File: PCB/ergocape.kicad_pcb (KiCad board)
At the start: 2 copper layers, 183.2 x 140.8 mm, 94 parts, among them J1 AudioJack4, J2 AudioJack4, SW1 SW_PUSH, U1 ATMEGA32U4, X1 Crystal_GND24_Small

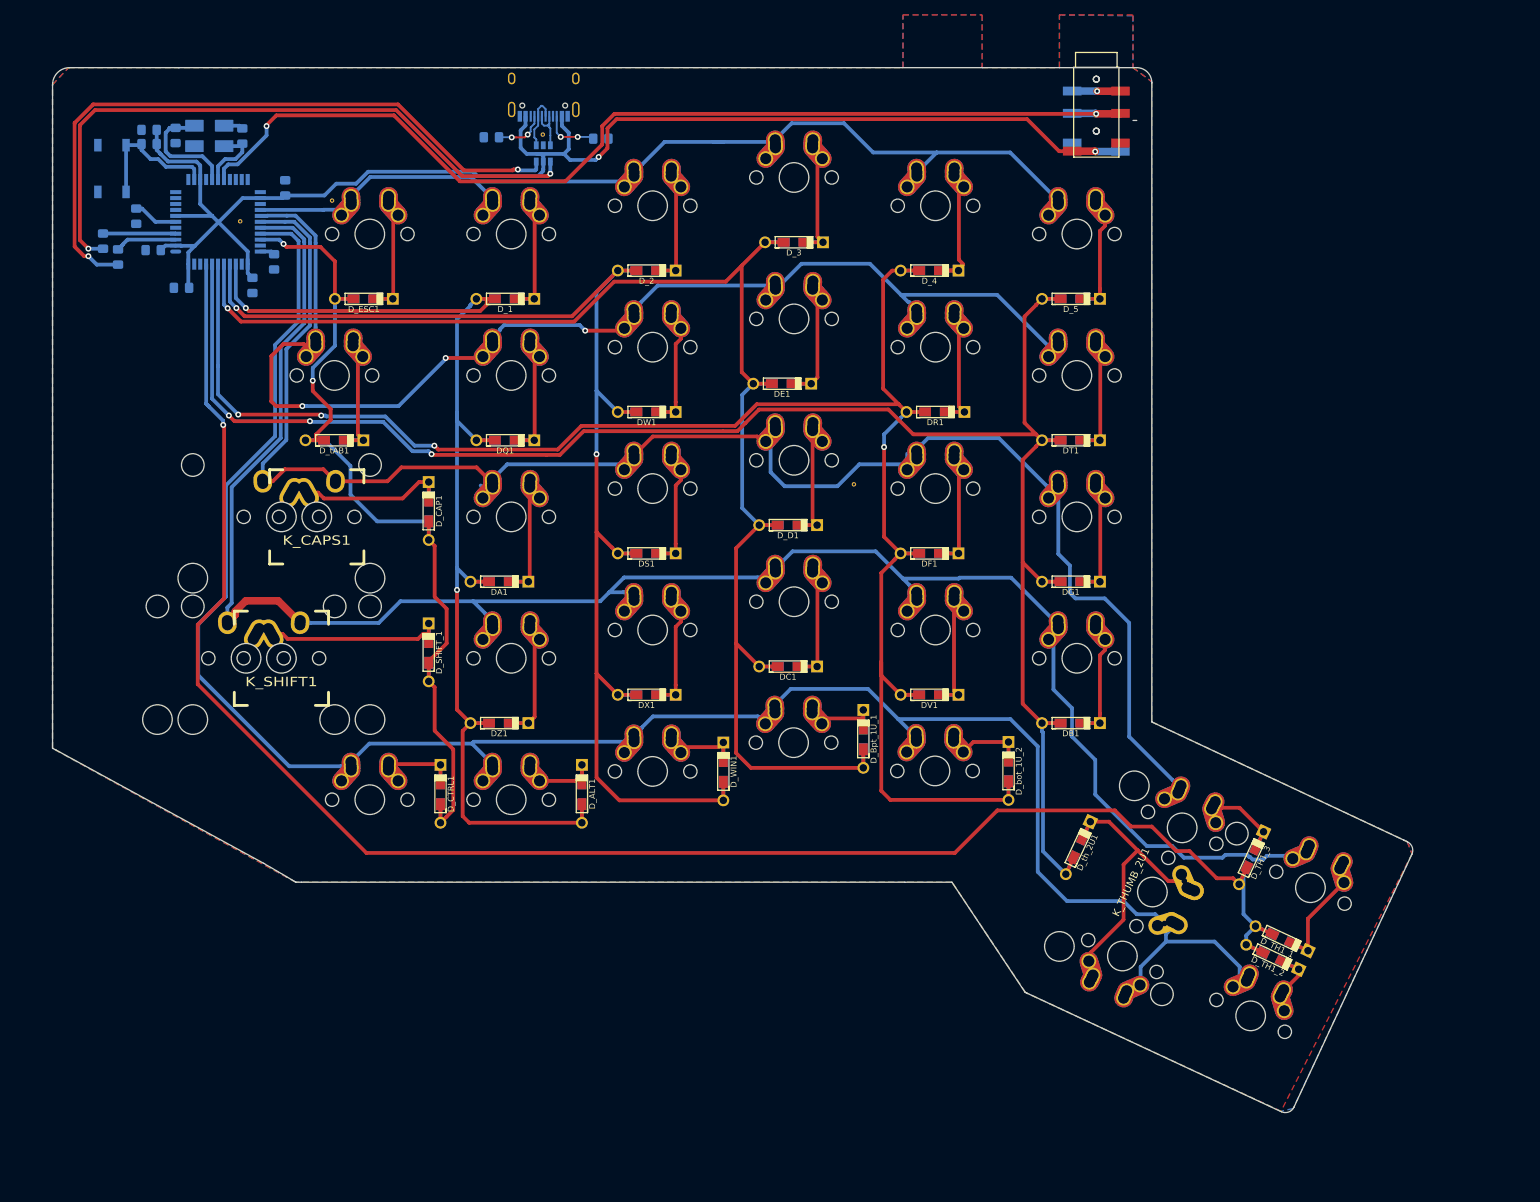
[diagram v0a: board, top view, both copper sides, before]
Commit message: added files for case files based of fr4 or similar.
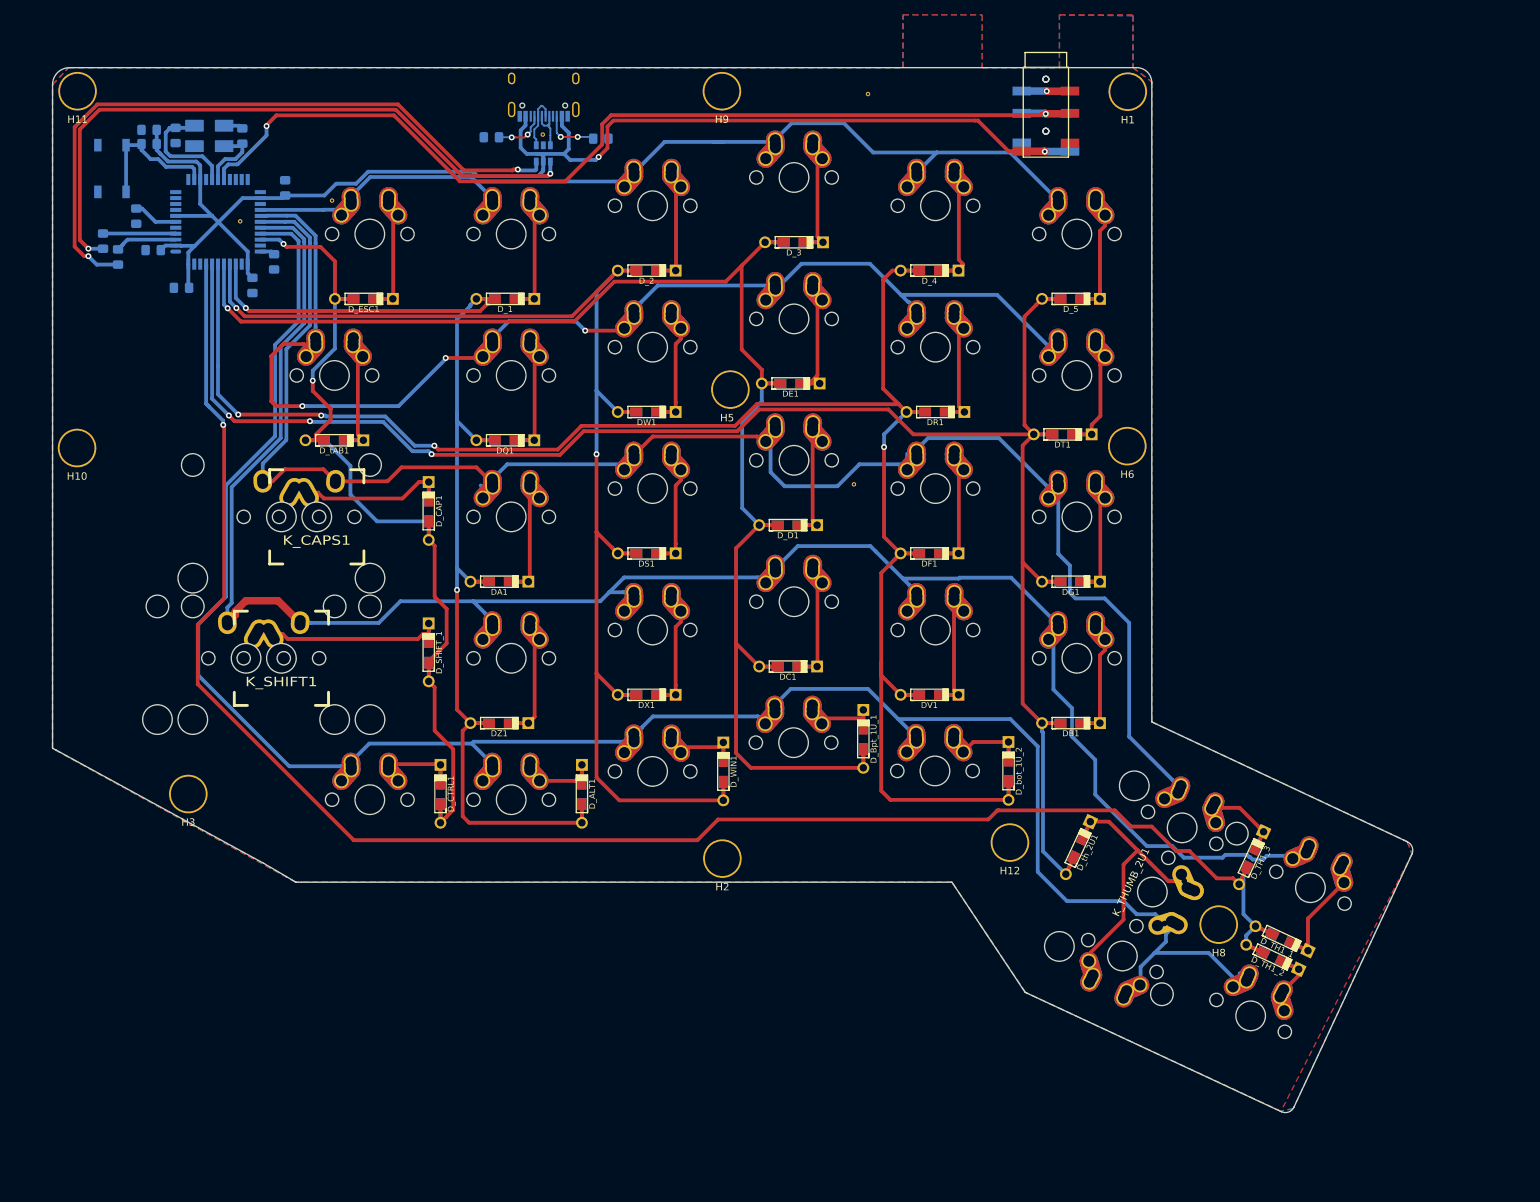
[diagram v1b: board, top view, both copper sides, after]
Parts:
- added H1: MountingHole, usbc_footprint:mounting_hole_4.7x5.2mm, F.Cu at (167.2, 20.5)
- added H10: MountingHole, usbc_footprint:mounting_hole_4.7x5.2mm, F.Cu at (25.7, 68.5)
- added H11: MountingHole, usbc_footprint:mounting_hole_4.7x5.2mm, F.Cu at (25.7, 20.4)
- added H12: MountingHole, usbc_footprint:mounting_hole_4.7x5.2mm, F.Cu at (151.3, 121.7)
- added H2: MountingHole, usbc_footprint:mounting_hole_4.7x5.2mm, F.Cu at (112.6, 123.8)
- added H3: MountingHole, usbc_footprint:mounting_hole_4.7x5.2mm, F.Cu at (40.6, 115.1)
- added H5: MountingHole, usbc_footprint:mounting_hole_4.7x5.2mm, F.Cu at (113.2, 60.6)
- added H6: MountingHole, usbc_footprint:mounting_hole_4.7x5.2mm, F.Cu at (167.1, 68.3)
- added H8: MountingHole, usbc_footprint:mounting_hole_4.7x5.2mm, F.Cu at (179.5, 132.7)
- added H9: MountingHole, usbc_footprint:mounting_hole_4.7x5.2mm, F.Cu at (112.5, 20.4)
- added REF**: via-0.6mm, usbc_footprint:via-0.6mm, F.Cu at (132.2, 20.8)
- moved J1 6.79 mm to (156.2, 17.2)
- moved J2 6.79 mm to (156.2, 17.2)
- moved DT1 1.37 mm to (158.4, 66.7)
- moved DE1 1.14 mm to (121.8, 59.8)
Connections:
- J1 pad R1: Net-(J1-PadR1) -> (no net)
- J2 pad R1: Net-(J2-PadR1) -> (no net)
- U1 pad 1: Net-(U1-Pad1) -> (no net)
- U1 pad 10: Net-(U1-Pad10) -> (no net)
- U1 pad 11: Net-(U1-Pad11) -> (no net)
- U1 pad 12: Net-(U1-Pad12) -> (no net)
- U1 pad 19: Net-(U1-Pad19) -> (no net)
- U1 pad 20: Net-(U1-Pad20) -> (no net)
- U1 pad 21: Net-(U1-Pad21) -> (no net)
- U1 pad 22: Net-(U1-Pad22) -> (no net)
- U1 pad 25: Net-(U1-Pad25) -> (no net)
- U1 pad 32: Net-(U1-Pad32) -> (no net)
- U1 pad 42: Net-(U1-Pad42) -> (no net)
- U1 pad 8: Net-(U1-Pad8) -> (no net)
- U1 pad 9: Net-(U1-Pad9) -> (no net)
- USB_1 pad 3: Net-(USB_1-Pad3) -> (no net)
- USB_1 pad 9: Net-(USB_1-Pad9) -> (no net)
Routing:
- net VCC: track 195.3 -> 188.4 mm
- net /SERIAL: track 138.2 -> 131.6 mm
- net /COL7: track 226.3 -> 224.9 mm
- net /COL6: track 222.8 -> 221.6 mm
- net /ROW5: track 263.6 -> 264.6 mm
- net /COL4: track 175.3 -> 176.2 mm
- net /ROW4: track 252.5 -> 253.0 mm
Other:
- outline, holes or cut-outs redrawn

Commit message: Change in layout and design, remove atmega32u4
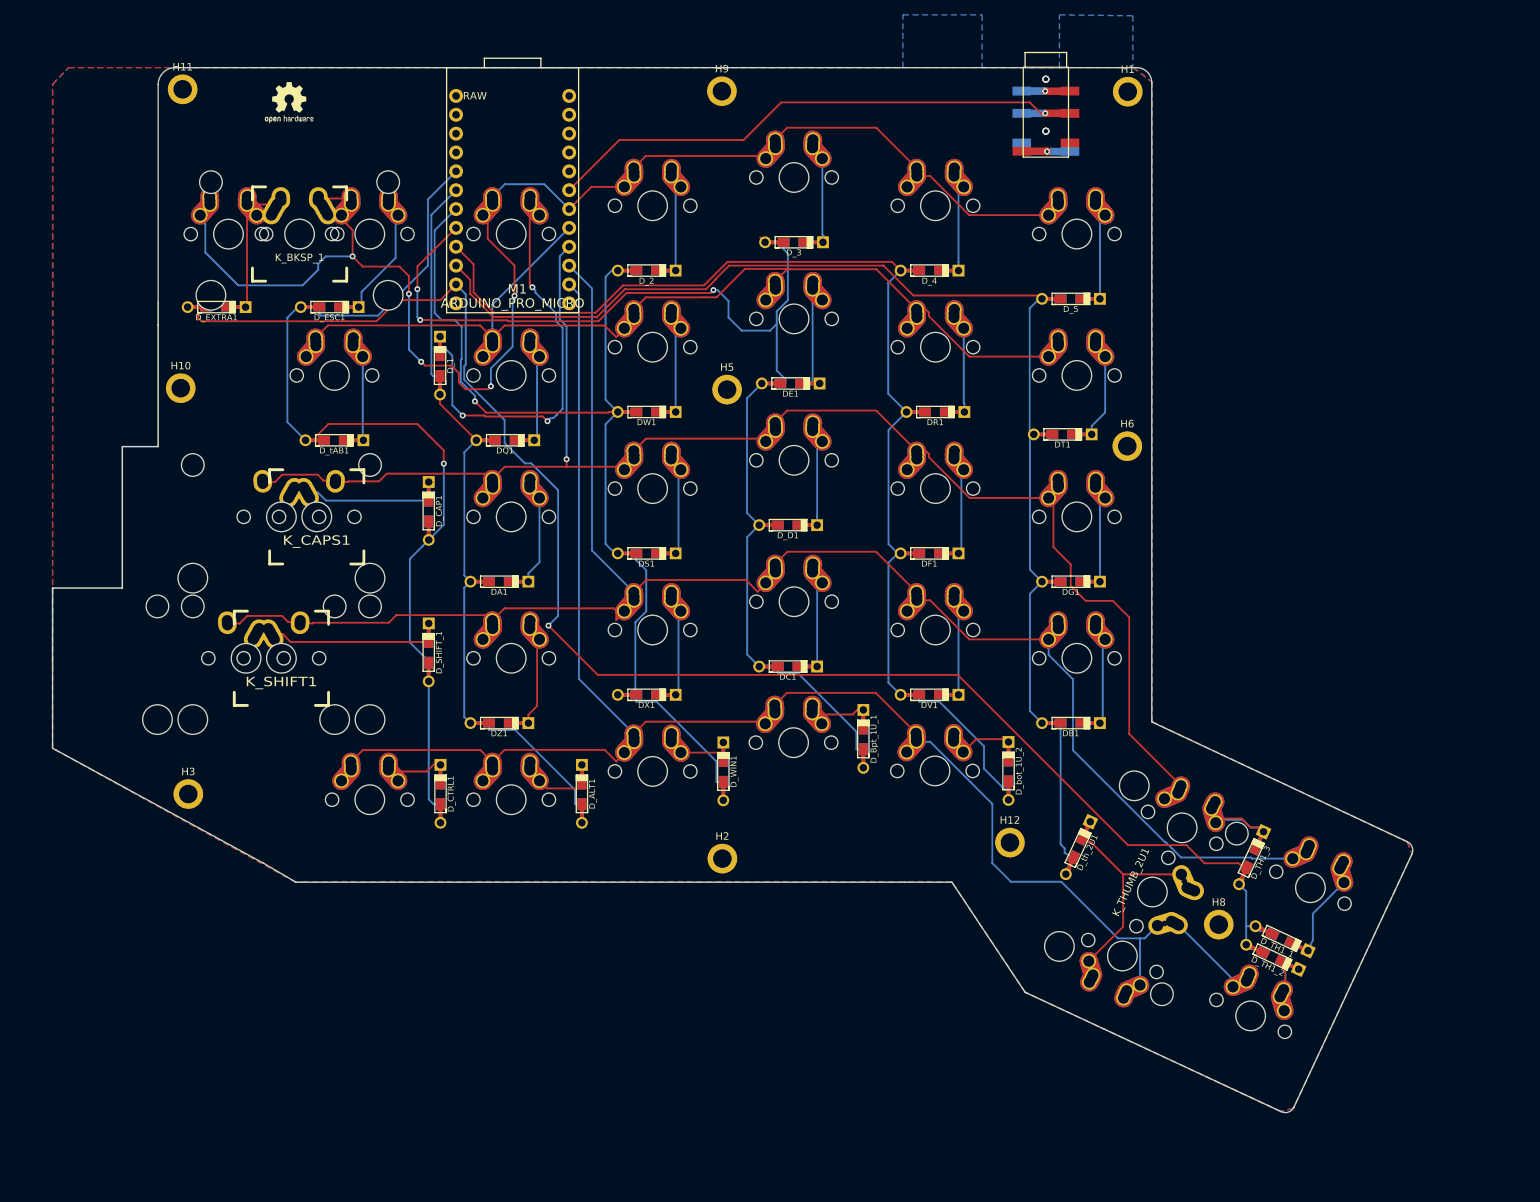
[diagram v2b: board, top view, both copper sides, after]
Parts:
- removed C1, C2: 22p, Capacitor_SMD:C_0805_2012Metric_Pad1.15x1.40mm_HandSolder
- removed C3, C4, C5, C6: 0.1u, Capacitor_SMD:C_0805_2012Metric_Pad1.15x1.40mm_HandSolder
- removed C7: 4.7u, Capacitor_SMD:C_0805_2012Metric_Pad1.15x1.40mm_HandSolder
- removed C8: 1u, Capacitor_SMD:C_0805_2012Metric_Pad1.15x1.40mm_HandSolder
- removed R1, R2: 10k, Resistor_SMD:R_0805_2012Metric_Pad1.15x1.40mm_HandSolder
- removed R3, R4: 22, Resistor_SMD:R_0805_2012Metric_Pad1.15x1.40mm_HandSolder
- removed the REF** at (47.6, 38.0)
- removed the REF** at (130.3, 73.4)
- removed the REF** at (60.0, 35.2)
- removed the REF** at (88.4, 26.3)
- removed the REF** at (132.2, 20.8)
- removed R_CC1, R_CC2: 5.1k, Resistor_SMD:R_0805_2012Metric_Pad1.15x1.40mm_HandSolder
- removed SW1: SW_PUSH, Button_Switch_SMD:SW_SPST_TL3342
- removed U1: ATMEGA32U4, acheron_Components:TQPF-44_10x10mm_P0.8mm
- removed USB_1: HRO-TYPE-C-31-M-12, usbc_footprint:HRO-TYPE-C-31-M-12
- removed U_ESD_1: USBLC6-2SC6, Package_TO_SOT_SMD:SOT-23-6
- removed X1: Crystal_GND24_Small, acheron_Components:Crystal_SMD_5032-4Pin-HandSolder
- added D_EXTRA1: D, Keebio-Parts:Diode-dual, F.Cu at (44.5, 49.5)
- added K_BKSP_1: KEYSW, Keebio-Parts:Hybrid_PCB_200H-dual, F.Cu at (55.6, 39.7)
- added K_XTRA1: KEYSW, Keebio-Parts:Hybrid_PCB_100H_Dual_hole, F.Cu at (46.1, 39.7)
- added M1: ARDUINO_PRO_MICRO, SparkFun-Boards:ARDUINO_PRO_MICRO, B.Cu at (84.3, 33.8)
- added REF**: OSHW-Logo2_7.3x6mm_SilkScreen, logo_lib:OSHW-Logo2_7.3x6mm_SilkScreen, B.Cu at (54.2, 22.0)
- added REF**: OSHW-Logo2_7.3x6mm_SilkScreen, logo_lib:OSHW-Logo2_7.3x6mm_SilkScreen, F.Cu at (54.2, 22.0)
- H1, H10, H11, H12, H2, H3, H5, H6, H8, H9: footprint usbc_footprint:mounting_hole_4.7x5.2mm -> acheron_MountingHoles:MountingHole_2.5x4.0mm
- moved H10 16.1 mm to (39.6, 60.5)
- moved H11 14.2 mm to (39.9, 20.2)
- moved D_1 12.6 mm to (74.5, 57.4), turned to 90 degrees
- moved D_ESC1 4.74 mm to (59.7, 49.5)
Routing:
- net VCC: track 188.4 -> 6.54 mm, vias 2 -> 1
- net /ROW1: track 123.8 -> 218.0 mm, vias 0 -> 5
- net /USB_D_N_OUT: track 91.3 -> 0.00 mm, vias 2 -> 0
- net /USB_D_P_OUT: track 88.4 -> 0.00 mm, vias 2 -> 0
- net /SERIAL: track 131.6 -> 76.1 mm, vias 2 -> 1
- net Net-(D_1-Pad1): track 12.0 -> 64.2 mm, vias 0 -> 3
- net /COL1: track 100.1 -> 145.9 mm, vias 2 -> 1
- net /COL5: track 215.7 -> 175.7 mm, vias 4 -> 0
- net Net-(D_EXTRA1-Pad1): track 0.00 -> 29.0 mm
- net /COL6: track 221.6 -> 192.7 mm, vias 3 -> 0
- net /ROW5: track 264.6 -> 245.0 mm
- net /RST: track 18.8 -> 0.00 mm
- net Net-(D_TH1_3-Pad1): track 8.51 -> 25.5 mm
- net /COL2: track 136.0 -> 119.5 mm, vias 2 -> 0
- net Net-(C2-Pad1): track 15.8 -> 0.00 mm
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- added copper zone on F.Cu, net VCC
- removed copper zone on F.Cu, net GND
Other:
- outline, holes or cut-outs redrawn

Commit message: cleanup and finish the case files
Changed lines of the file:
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@@
     (thickness 1.6)
     (drawings 34)
-    (tracks 1741)
+    (tracks 1743)
     (zones 0)
     (modules 87)
@@
     (38 B.Mask user)
     (39 F.Mask user)
-    (40 Dwgs.User user hide)
+    (40 Dwgs.User user)
     (41 Cmts.User user)
     (42 Eco1.User user)
     (43 Eco2.User user)
     (44 Edge.Cuts user)
-    (45 Margin user)
+    (45 Margin user hide)
     (46 B.CrtYd user hide)
     (47 F.CrtYd user hide)
@@
   )
   (setup
-    (last_trace_width 1.016)
+    (last_trace_width 0.25)
     (user_trace_width 0.508)
     (user_trace_width 1.016)
@@
     (mod_text_size 1 1)
     (mod_text_width 0.15)
-    (pad_size 0.6 0.6)
-    (pad_drill 0.3)
+    (pad_size 4 4)
+    (pad_drill 2.5)
     (pad_to_mask_clearance 0.051)
     (solder_mask_min_width 0.25)
@@
       (drillshape 0)
       (scaleselection 1)
-      (outputdirectory "ergocape_v3"))
+      (outputdirectory "ergocape_v4"))
   )
   (net 0 "")
@@
       (effects (font (size 1 1) (thickness 0.15)))
     )
-    (pad 1 thru_hole circle (at 0 0) (size 4 4) (drill 2.5) (layers *.Cu *.Mask))
+    (pad 1 thru_hole circle (at 0.699 0.0635) (size 4 4) (drill 2.5) (layers *.Cu *.Mask))
   )
   (module acheron_MountingHoles:MountingHole_2.5x4.0mm (layer F.Cu)
@@
   (segment (start 117.544 97.9488) (end 118.944 97.9488) (width 0.25) (layer F.Cu) (net 7))
   (segment (start 118.944 97.9488) (end 120.044 97.9488) (width 0.25) (layer F.Cu) (net 7))
-  (segment (start 117.893 59.817) (end 115.9059 61.8041) (width 0.25) (layer B.Cu) (net 7))
-  (segment (start 115.9059 61.8041) (end 115.9059 77.2607) (width 0.25) (layer B.Cu) (net 7))
   (segment (start 115.9059 77.2607) (end 117.544 78.8988) (width 0.25) (layer B.Cu) (net 7))
   (segment (start 117.893 59.817) (end 119.293 59.817) (width 0.25) (layer B.Cu) (net 7))
@@
   (segment (start 119.9043 50.1087) (end 119.9043 51.816) (width 0.25) (layer B.Cu) (net 7))
   (segment (start 119.9043 51.816) (end 119.9043 58.0713) (width 0.25) (layer B.Cu) (net 7))
+  (segment (start 115.9059 62.93547) (end 115.9059 63.5) (width 0.25) (layer B.Cu) (net 7))
+  (segment (start 117.893 60.94837) (end 115.9059 62.93547) (width 0.25) (layer B.Cu) (net 7))
+  (segment (start 117.893 59.817) (end 117.893 60.94837) (width 0.25) (layer B.Cu) (net 7))
+  (segment (start 115.9059 63.5) (end 115.9059 77.2607) (width 0.25) (layer B.Cu) (net 7))
   (segment (start 124.738 40.7988) (end 123.638 40.7988) (width 0.25) (layer B.Cu) (net 8))
   (segment (start 125.438 40.7988) (end 124.738 40.7988) (width 0.25) (layer B.Cu) (net 8))

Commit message: add renders
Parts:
- M1: value ARDUINO_PRO_MICRO -> >VALUE
- moved D_EXTRA1 1.70 mm to (44.5, 51.2)
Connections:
- J1 pad R1: (no net) -> Net-(J1-PadR1)
- J2 pad R1: (no net) -> Net-(J2-PadR1)
- M1 pad 1: (no net) -> Net-(M1-Pad1)
- M1 pad 12: (no net) -> Net-(M1-Pad12)
- M1 pad 13: (no net) -> Net-(M1-Pad13)
- M1 pad 2: (no net) -> Net-(M1-Pad2)
- M1 pad 22: (no net) -> Net-(M1-Pad22)
- M1 pad 24: (no net) -> Net-(M1-Pad24)
- M1 pad 5: (no net) -> Net-(M1-Pad5)
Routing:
- net /COL7: track 229.8 -> 224.9 mm
- net Net-(D_EXTRA1-Pad1): track 29.0 -> 27.8 mm
